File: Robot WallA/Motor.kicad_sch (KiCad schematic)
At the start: 0 parts

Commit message: Continued to link MCU pins, Added a sheet for servomotors and optional 2 DC motors.
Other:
- sheet Motor_Actuators ports: added 3V3; removed none
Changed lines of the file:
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@@
+		)
+	)
+	(wire
+		(pts
+			(xy 26.67 22.86) (xy 33.02 22.86)
+		)
+		(stroke
+			(width 0)
+			(type default)
 		)
 	)
@@
 		)
 	)
+	(label "SERVO_PWM2"
+		(at 118.11 173.99 180)
+		(effects
+			(font
+				(size 1.27 1.27)
+			)
+			(justify right bottom)
+		)
+	)
 	(label "WHEEL_SLEEP"
 		(at 210.82 57.15 180)
@@
 		)
 	)
-	(label "PWM1"
-		(at 118.11 171.45 180)
-		(effects
-			(font
-				(size 1.27 1.27)
-			)
-			(justify right bottom)
-		)
-	)
 	(label "WHEEL_NFAULT"
 		(at 69.85 64.77 180)
@@
 		)
 	)
-	(label "PWM3"
-		(at 118.11 176.53 180)
-		(effects
-			(font
-				(size 1.27 1.27)
-			)
-			(justify right bottom)
-		)
-	)
-	(label "PWM4"
-		(at 118.11 179.07 180)
-		(effects
-			(font
-				(size 1.27 1.27)
-			)
-			(justify right bottom)
-		)
-	)
 	(label "SERVO_RX_UC"
 		(at 64.77 124.46 180)
@@
 		)
 	)
+	(label "SERVO_PWM4"
+		(at 118.11 179.07 180)
+		(effects
+			(font
+				(size 1.27 1.27)
+			)
+			(justify right bottom)
+		)
+	)
 	(label "WHEEL6"
 		(at 78.74 64.77 180)
@@
 		)
 	)
+	(label "SERVO_PWM1"
+		(at 118.11 171.45 180)
+		(effects
+			(font
+				(size 1.27 1.27)
+			)
+			(justify right bottom)
+		)
+	)
 	(label "CurrentSenseMotor2"
 		(at 69.85 52.07 180)
@@
 		)
 	)
+	(label "SERVO_PWM3"
+		(at 118.11 176.53 180)
+		(effects
+			(font
+				(size 1.27 1.27)
+			)
+			(justify right bottom)
+		)
+	)
 	(label "WHEEL_PWM1"
 		(at 69.85 54.61 180)
@@
 		)
 	)
+	(label "3V3"
+		(at 33.02 22.86 0)
+		(effects
+			(font
+				(size 1.27 1.27)
+			)
+			(justify left bottom)
+		)
+	)
 	(label "WHEEL_PWM3"
 		(at 210.82 46.99 180)
@@
 		)
 	)
+	(label "3V3"
+		(at 118.11 140.97 180)
+		(effects
+			(font
+				(size 1.27 1.27)
+			)
+			(justify right bottom)
+		)
+	)
 	(label "SERVO3"
 		(at 73.66 132.08 180)
@@
 		)
 	)
-	(label "PWM2"
-		(at 118.11 173.99 180)
+	(label "3V3"
+		(at 210.82 22.86 180)
 		(effects
 			(font
@@
 	(hierarchical_label "3V3"
 		(shape input)
-		(at 210.82 22.86 180)
+		(at 26.67 22.86 180)
 		(effects
 			(font
@@
 		)
 		(instances
-			(project "PCB"
+			(project "Robot WallA"
 				(path "/117fd49e-499d-4b54-b58c-f6b538ecca4a/a16960dc-56f6-4cf6-af27-6c174f94c7f8"
 					(page "16")
@@
 			)
 		)
+		(pin "3V3" input
+			(at 118.11 140.97 180)
+			(effects
+				(font
+					(size 1.27 1.27)
+				)
+				(justify left)
+			)
+		)
 		(instances
-			(project "PCB"
+			(project "Robot WallA"
 				(path "/117fd49e-499d-4b54-b58c-f6b538ecca4a/a16960dc-56f6-4cf6-af27-6c174f94c7f8"
 					(page "4")
@@
 		)
 		(instances
-			(project "PCB"
+			(project "Robot WallA"
 				(path "/117fd49e-499d-4b54-b58c-f6b538ecca4a/a16960dc-56f6-4cf6-af27-6c174f94c7f8"
 					(page "12")

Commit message: Defined every footprints
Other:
- sheet Motor_Actuators ports: added CurrentSense1, CurrentSense2, IN1, IN2, IN3, IN4, PWM5, PWM6; removed none

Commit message: Added standard switchs, debug leds and 12V and 5V connectors
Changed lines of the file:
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@@
 		)
 	)
-	(label "SERVO_TX_ENABLE"
+	(label "SERVO_ROBOTIS_TX_ENABLE"
 		(at 148.59 33.02 180)
 		(effects
@@
 		)
 	)
-	(label "SERVO_TX_ENABLE"
+	(label "SERVO_ROBOTIS_TX_ENABLE"
 		(at 71.12 149.86 180)
 		(effects

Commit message: Conitnue routing
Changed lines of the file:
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@@
 			)
 		)
-		(pin "ENCODER_LEFT_1" input
+		(pin "ENCODER_LEFT_1" output
 			(at 137.16 76.2 180)
 			(effects
@@
 			)
 		)
-		(pin "ENCODER_LEFT_2" input
+		(pin "ENCODER_LEFT_2" output
 			(at 137.16 78.74 180)
 			(effects
@@
 			)
 		)
-		(pin "ENCODER_RIGHT_1" input
+		(pin "ENCODER_RIGHT_1" output
 			(at 137.16 83.82 180)
 			(effects
@@
 			)
 		)
-		(pin "ENCODER_RIGHT_2" input
+		(pin "ENCODER_RIGHT_2" output
 			(at 137.16 86.36 180)
 			(effects

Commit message: Updated fab files.
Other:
- company: (none) -> Socotec Monitoring
- title: (none) -> Robot Wall-A
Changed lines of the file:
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@@
 	(generator_version "9.0")
 	(paper "A4")
+	(title_block
+		(title "Robot Wall-A")
+		(date "2025-09-20")
+		(rev "v1.0")
+		(company "Socotec Monitoring")
+		(comment 1 "GDU")
+		(comment 2 "THO")
+	)
 	(bus_entry
 		(at 81.28 29.21)

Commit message: Modified a bit pin header pins to allow I2C,SPI and CAN
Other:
- sheet Motor_WheelDriver ports: added ADC_PRI_MOTOR_CURRENT_1, ADC_PRI_MOTOR_CURRENT_2; removed CurrentSenseMotor1, CurrentSenseMotor2
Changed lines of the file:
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@@
 		)
 	)
-	(label "WHEEL_SLEEP"
+	(label "PRI_MOTOR_SLEEP"
 		(at 44.45 96.52 180)
 		(effects
@@
 		)
 	)
-	(label "SECONDARY_MOTOR_CURRENT2"
+	(label "ADC_SEC_MOTOR_CURRENT_2"
 		(at 199.39 30.48 180)
 		(effects
@@
 		)
 	)
-	(label "WHEEL_NFAULT"
+	(label "PRI_MOTOR_NFAULT"
 		(at 68.58 41.91 180)
 		(effects
@@
 		)
 	)
-	(label "SECONDARY_MOTOR_CURRENT1"
+	(label "ADC_SEC_MOTOR_CURRENT_1"
 		(at 127 132.08 0)
 		(effects
@@
 		)
 	)
-	(label "WHEEL_NFAULT"
+	(label "PRI_MOTOR_NFAULT"
 		(at 44.45 93.98 180)
 		(effects
@@
 		)
 	)
-	(label "CurrentSenseMotor2"
+	(label "ADC_PRI_MOTOR_CURRENT_2"
 		(at 68.58 29.21 180)
 		(effects
@@
 		)
 	)
-	(label "SECONDARY_MOTOR_CURRENT1"
+	(label "ADC_SEC_MOTOR_CURRENT_1"
 		(at 199.39 27.94 180)
 		(effects
@@
 		)
 	)
-	(label "CurrentSenseMotor1"
+	(label "ADC_PRI_MOTOR_CURRENT_1"
 		(at 44.45 73.66 180)
 		(effects
@@
 		)
 	)
-	(label "SECONDARY_MOTOR_CURRENT2"
+	(label "ADC_SEC_MOTOR_CURRENT_2"
 		(at 127 134.62 0)
 		(effects
@@
 		)
 	)
-	(label "CurrentSenseMotor2"
+	(label "ADC_PRI_MOTOR_CURRENT_2"
 		(at 44.45 76.2 180)
 		(effects
@@
 		)
 	)
-	(label "WHEEL_SLEEP"
+	(label "PRI_MOTOR_SLEEP"
 		(at 68.58 44.45 180)
 		(effects
@@
 		)
 	)
-	(label "CurrentSenseMotor1"
+	(label "ADC_PRI_MOTOR_CURRENT_1"
 		(at 68.58 26.67 180)
 		(effects
@@
 			)
 		)
-		(pin "CurrentSenseMotor1" output
+		(pin "ADC_PRI_MOTOR_CURRENT_1" output
 			(at 44.45 73.66 180)
 			(effects
@@
 			)
 		)
-		(pin "CurrentSenseMotor2" output
+		(pin "ADC_PRI_MOTOR_CURRENT_2" output
 			(at 44.45 76.2 180)
 			(effects

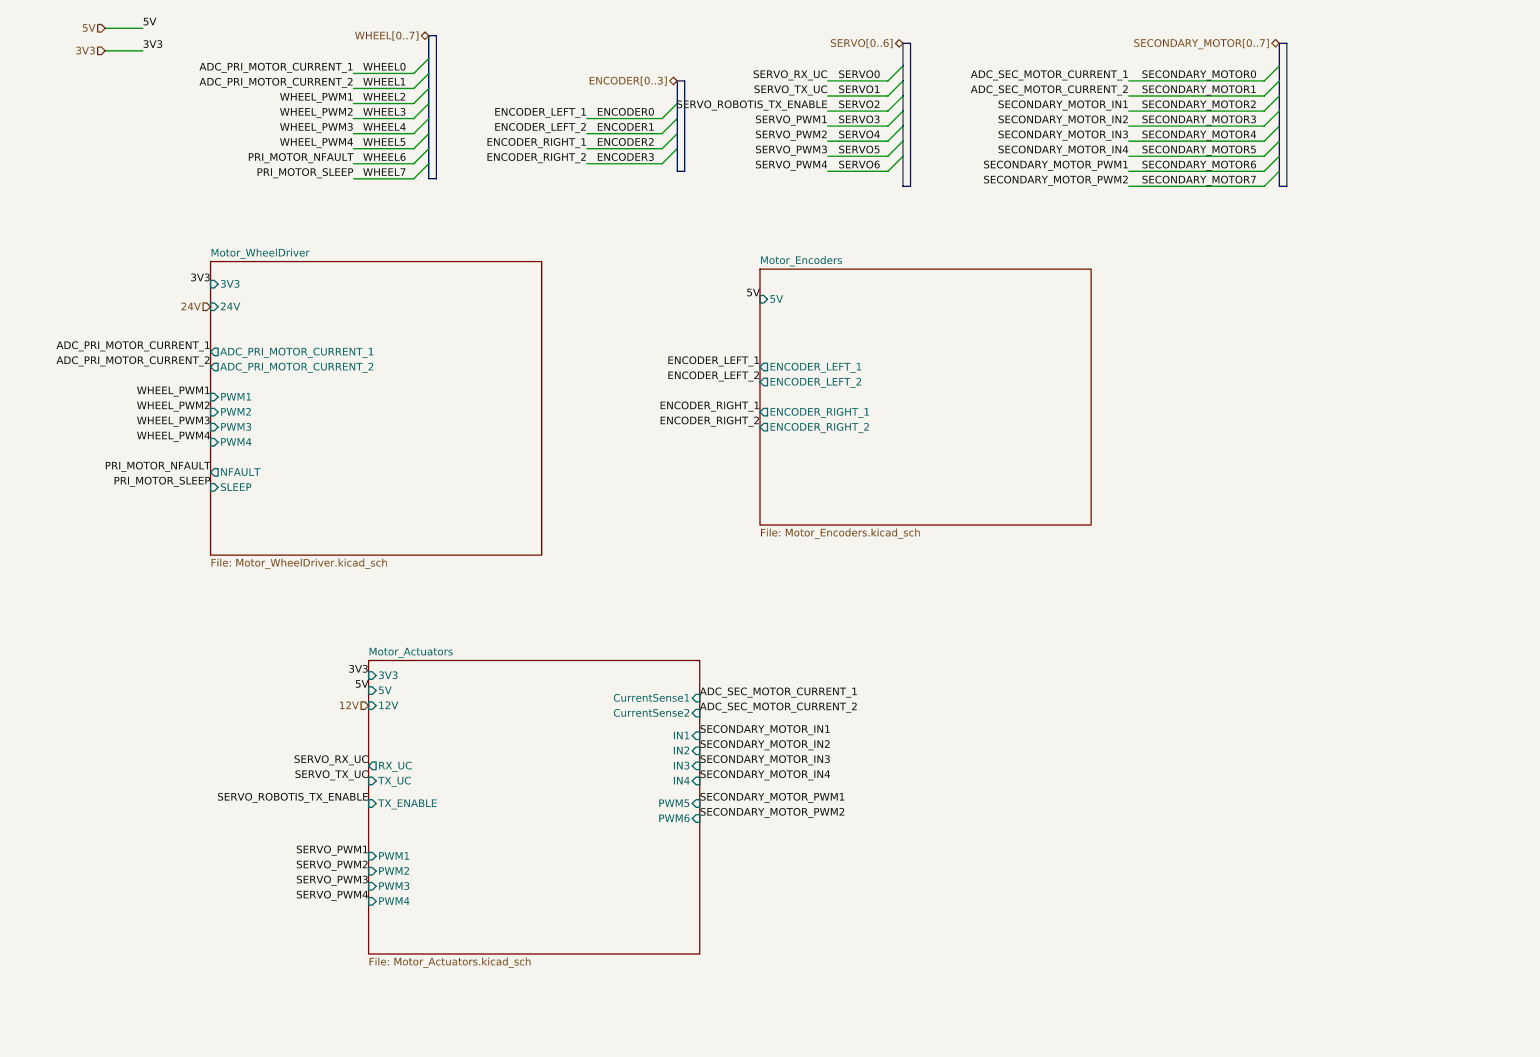
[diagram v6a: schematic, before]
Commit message: Added 3 thermistor to measure temperature near 12V and 24V power supplies and near motor drivers
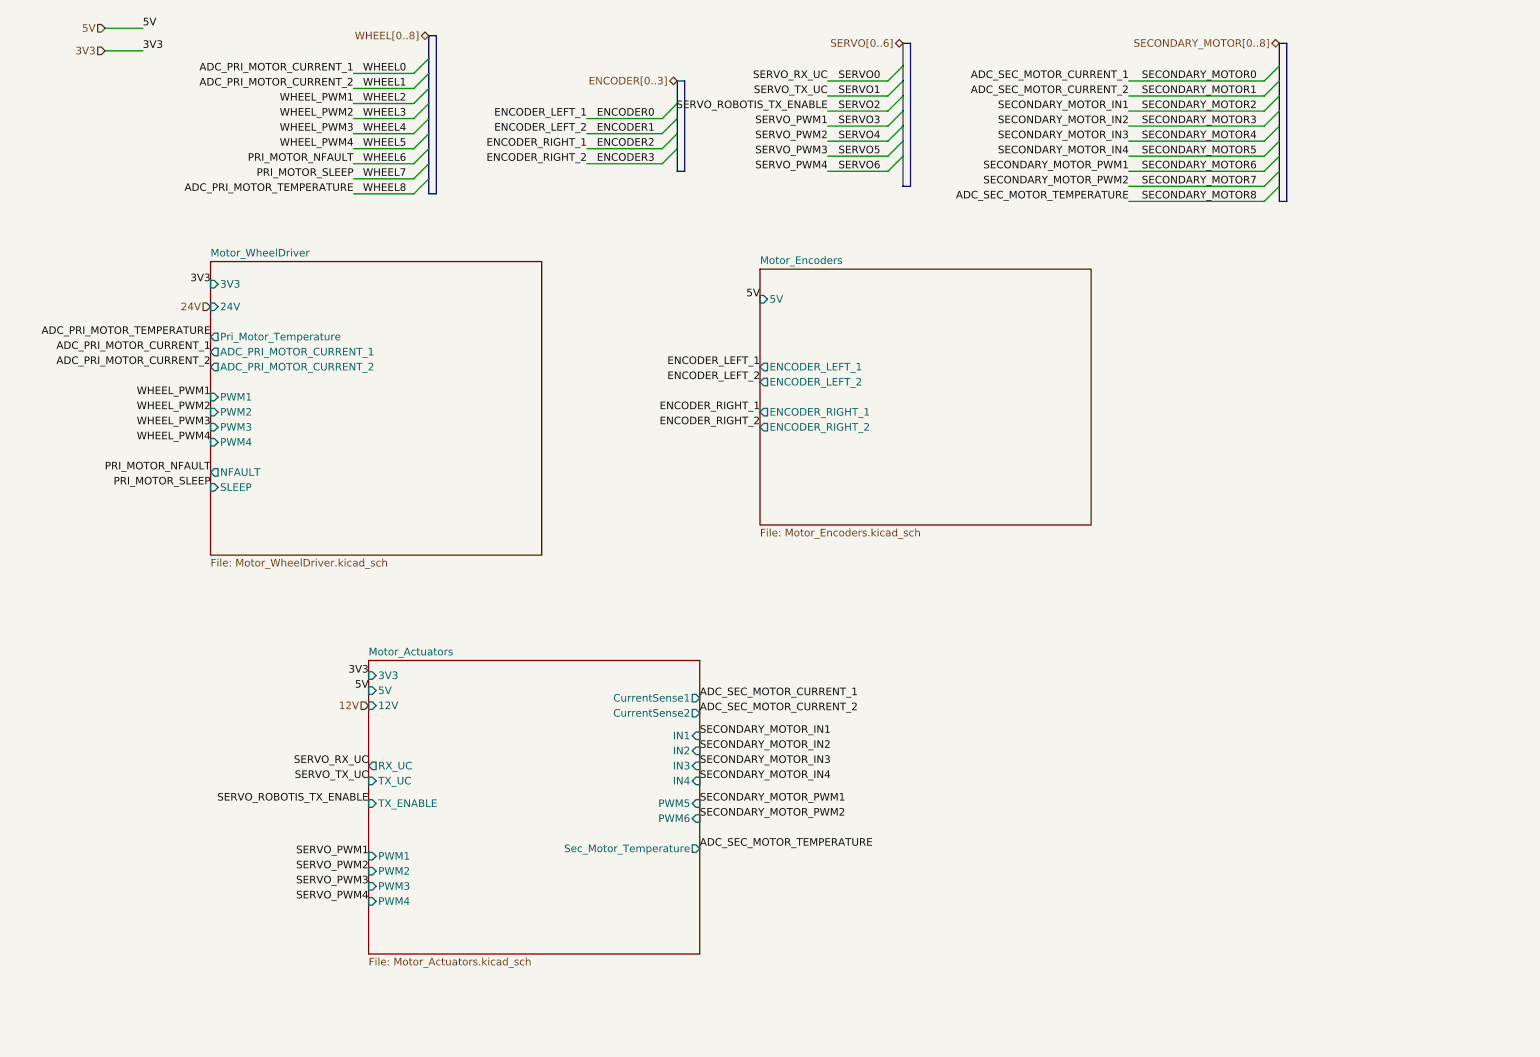
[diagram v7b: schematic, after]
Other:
- sheet Motor_Actuators ports: added Sec_Motor_Temperature; removed none
- sheet Motor_WheelDriver ports: added Pri_Motor_Temperature; removed none
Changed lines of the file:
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@@
+	)
+	(bus_entry
+		(at 81.28 44.45)
+		(size -2.54 2.54)
+		(stroke
+			(width 0)
+			(type default)
+		)
 	)
 	(bus_entry
@@
 	)
 	(bus_entry
+		(at 224.79 45.72)
+		(size -2.54 2.54)
+		(stroke
+			(width 0)
+			(type default)
+		)
+	)
+	(bus_entry
 		(at 81.28 41.91)
 		(size -2.54 2.54)
@@
 	(wire
 		(pts
+			(xy 68.58 46.99) (xy 78.74 46.99)
+		)
+		(stroke
+			(width 0)
+			(type default)
+		)
+	)
+	(wire
+		(pts
 			(xy 148.59 30.48) (xy 158.75 30.48)
 		)
@@
 	(bus
 		(pts
-			(xy 82.55 20.32) (xy 82.55 44.45)
+			(xy 82.55 20.32) (xy 82.55 46.99)
 		)
 		(stroke
@@
 	(bus
 		(pts
-			(xy 226.06 21.59) (xy 226.06 45.72)
+			(xy 226.06 21.59) (xy 226.06 48.26)
 		)
 		(stroke
@@
 	(bus
 		(pts
-			(xy 224.79 45.72) (xy 226.06 45.72)
+			(xy 224.79 48.26) (xy 226.06 48.26)
 		)
 		(stroke
@@
 	(bus
 		(pts
+			(xy 81.28 44.45) (xy 81.28 46.99)
+		)
+		(stroke
+			(width 0)
+			(type default)
+		)
+	)
+	(wire
+		(pts
+			(xy 199.39 48.26) (xy 222.25 48.26)
+		)
+		(stroke
+			(width 0)
+			(type default)
+		)
+	)
+	(bus
+		(pts
 			(xy 81.28 31.75) (xy 81.28 34.29)
 		)
@@
 		)
 	)
+	(bus
+		(pts
+			(xy 224.79 45.72) (xy 224.79 48.26)
+		)
+		(stroke
+			(width 0)
+			(type default)
+		)
+	)
 	(wire
 		(pts
@@
 	(bus
 		(pts
-			(xy 81.28 44.45) (xy 82.55 44.45)
+			(xy 81.28 46.99) (xy 82.55 46.99)
 		)
 		(stroke
@@
 		)
 	)
+	(label "ADC_SEC_MOTOR_TEMPERATURE"
+		(at 199.39 48.26 180)
+		(effects
+			(font
+				(size 1.27 1.27)
+			)
+			(justify right bottom)
+		)
+	)
 	(label "PRI_MOTOR_SLEEP"
 		(at 44.45 96.52 180)
@@
 		)
 	)
+	(label "WHEEL8"
+		(at 77.47 46.99 180)
+		(effects
+			(font
+				(size 1.27 1.27)
+			)
+			(justify right bottom)
+		)
+	)
 	(label "SERVO_RX_UC"
 		(at 148.59 27.94 180)
@@
 		)
 	)
+	(label "SECONDARY_MOTOR8"
+		(at 220.98 48.26 180)
+		(effects
+			(font
+				(size 1.27 1.27)
+			)
+			(justify right bottom)
+		)
+	)
 	(label "SERVO_PWM4"
 		(at 71.12 166.37 180)
@@
 		)
 	)
+	(label "ADC_PRI_MOTOR_TEMPERATURE"
+		(at 68.58 46.99 180)
+		(effects
+			(font
+				(size 1.27 1.27)
+			)
+			(justify right bottom)
+		)
+	)
 	(label "SERVO_PWM4"
 		(at 148.59 43.18 180)
@@
 		)
 	)
+	(label "ADC_SEC_MOTOR_TEMPERATURE"
+		(at 127 157.48 0)
+		(effects
+			(font
+				(size 1.27 1.27)
+			)
+			(justify left bottom)
+		)
+	)
 	(label "3V3"
 		(at 33.02 22.86 0)
@@
 	(label "WHEEL7"
 		(at 77.47 44.45 180)
+		(effects
+			(font
+				(size 1.27 1.27)
+			)
+			(justify right bottom)
+		)
+	)
+	(label "ADC_PRI_MOTOR_TEMPERATURE"
+		(at 44.45 71.12 180)
 		(effects
 			(font
@@
 		)
 	)
-	(hierarchical_label "SECONDARY_MOTOR[0..7]"
+	(hierarchical_label "SECONDARY_MOTOR[0..8]"
 		(shape bidirectional)
 		(at 224.79 21.59 180)
@@
 		)
 	)
-	(hierarchical_label "WHEEL[0..7]"
+	(hierarchical_label "WHEEL[0..8]"
 		(shape bidirectional)
 		(at 81.28 20.32 180)
@@
 			)
 		)
-		(pin "CurrentSense1" input
+		(pin "CurrentSense1" output
 			(at 127 132.08 0)
 			(effects
@@
 			)
 		)
-		(pin "CurrentSense2" input
+		(pin "CurrentSense2" output
 			(at 127 134.62 0)
 			(effects
@@
 		(pin "PWM6" input
 			(at 127 152.4 0)
+			(effects
+				(font
+					(size 1.27 1.27)
+				)
+				(justify right)
+			)
+		)
+		(pin "Sec_Motor_Temperature" output
+			(at 127 157.48 0)
 			(effects
 				(font
@@
 			(effects
 				(font
+					(size 1.27 1.27)
+				)
+				(justify left)
+			)
+		)
+		(pin "Pri_Motor_Temperature" output
+			(at 44.45 71.12 180)
+			(effects
+				(font
